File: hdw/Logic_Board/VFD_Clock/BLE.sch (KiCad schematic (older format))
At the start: 17 parts, among them Q2701 BSS214NW, U2701 RN4871, U2702 74LVC1G97, U2703 74LVC1G97

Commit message: Started routing
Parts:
- removed C2703, C2704: 0.1uF, Capacitors_SMD:C_0603, symbol Custom_Library:C_Custom
- removed D2701: Red, LEDs:LED_0603, symbol Device:LED
- removed D2702: Yellow, LEDs:LED_0603, symbol Device:LED
- removed R2705: 10k, Resistors_SMD:R_0603, symbol Custom_Library:R_Custom
- removed R2706, R2707: 1k, Resistors_SMD:R_0603, symbol Custom_Library:R_Custom
- removed U2702: 74LVC1G97, Package_TO_SOT_SMD:SOT-363_SC-70-6, symbol Custom_Library:74LVC1G97_Power_BUF
- removed U2703: 74LVC1G97, Package_TO_SOT_SMD:SOT-363_SC-70-6, symbol Custom_Library:74LVC1G97_Power_AND

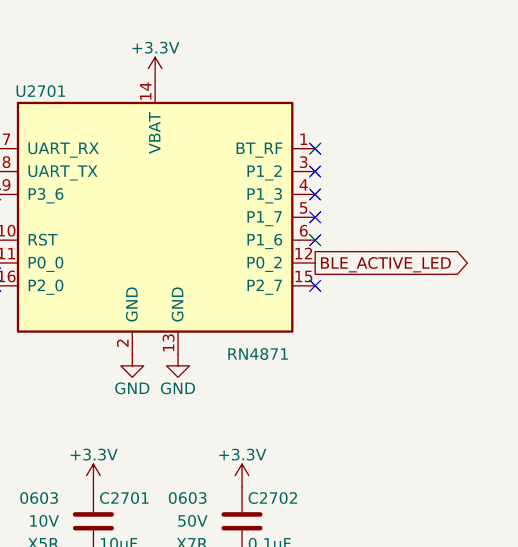
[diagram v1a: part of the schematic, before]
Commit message: Started display board PCB
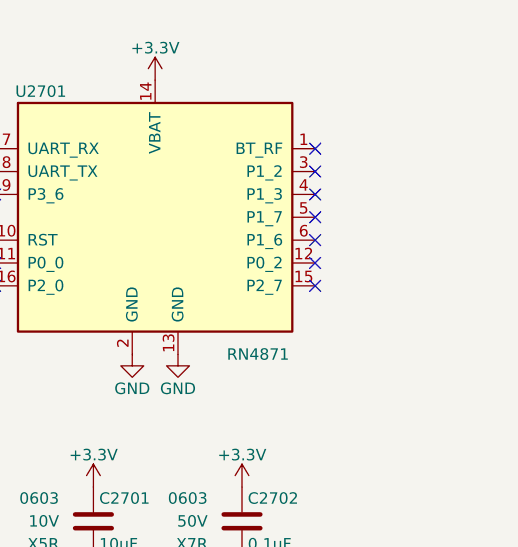
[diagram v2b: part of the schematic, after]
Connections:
- net BLE_ACTIVE_LED: no longer names the net of U2701.12 (P0_2)
- no-connect marks 9 -> 10
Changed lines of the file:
@@
 Text GLabel 2630 3480 0    50   Output ~ 0
 BLE_UART_RX
-Text GLabel 5830 3880 2    50   Output ~ 0
-BLE_ACTIVE_LED
 $Comp
 L Custom_Library:R_Custom R2701
@@
 NoConn ~ 4430 3880
 NoConn ~ 4430 3980
+NoConn ~ 5830 3880
 $EndSCHEMATC
